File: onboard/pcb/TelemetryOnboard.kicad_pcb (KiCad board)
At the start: 4 copper layers, 100 x 91 mm, 80 parts, among them J1 90 Deg. Socket 02x03 2.54mm, J2 Socket 01x02 2.54mm, J3 CONSMA001-SMD-G-T, J4 Socket 01x04 2.54mm, J5 Socket 01x02 2.54mm, U1 AVR128DB64x-xPT, U2 RC1780HP-RC232

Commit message: first version new schematic
added symbols, footprints, 3dmodels, added new pcb base layout, added first schematic elements
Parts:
- removed C5: 1nF, Capacitor_SMD:C_0805_2012Metric_Pad1.18x1.45mm_HandSolder
- removed D14, D15, D16: LED 0805 red, LED_SMD:LED_0805_2012Metric_Pad1.15x1.40mm_HandSolder
- removed J3: CONSMA001-SMD-G-T, Footprints:SMA Connector CONSMA001-SMD-G-T
- removed J4: Socket 01x04 2.54mm, Connector_PinSocket_2.54mm:PinSocket_1x04_P2.54mm_Vertical
- removed J5: Socket 01x02 2.54mm, Connector_PinSocket_2.54mm:PinSocket_1x02_P2.54mm_Vertical
- removed LS1: CMT-0525-75-SMT-TR, Footprints:Buzzer XDCR_CMT-0525-75-SMT-TR
- removed TP10, TP11, TP12, TP13, TP14, TP15, TP16, TP17, TP4, TP5, TP6, TP7, TP8, TP9: ~, Footprints:Test Point
- removed ZP1, ZS1: ~, Resistor_SMD:R_0805_2012Metric_Pad1.20x1.40mm_HandSolder
- added D3: orange, LED_SMD:LED_0805_2012Metric_Pad1.15x1.40mm_HandSolder, F.Cu at (11.8, 43.0)
- added D4: Cree RGB LED, Footprints:Cree RGB LED, F.Cu at (6.50, 41.0)
- added JP2: SolderJumper_2_Open, Footprints:Solder Jumper, F.Cu at (-20.1, 26.6)
- added R22: 560 Ohm, Resistor_SMD:R_0805_2012Metric, F.Cu at (-35.1, -33.5)
- added REF**: Test Point Hole, Footprints:Test Point Hole, F.Cu at (-24.5, 22.5)
- added REF**: Test Point Hole, Footprints:Test Point Hole, F.Cu at (-10.0, 22.5)
- added REF**: Test Point Hole, Footprints:Test Point Hole, F.Cu at (-13.0, 22.5)
- C1, C3: value 1uF -> 4.7 uF
- C2, C4: value 1uF -> 0.1 uF
- D1, D7: value LED 0805 orange -> orange
- D10: value LED 0805 green -> orange
- D11: value LED 0805 green -> BAT43; footprint LED_SMD:LED_0805_2012Metric_Pad1.15x1.40mm_HandSolder -> Diode_SMD:D_SOD-123
- D12: value LED 0805 green -> green
- D13: value LED 0805 red -> green
- D2: value CLS6B-FKW -> orange; footprint Footprints:RGB LED Cree-PLCC-6_6x5mm_P2.1mm -> LED_SMD:LED_0805_2012Metric_Pad1.15x1.40mm_HandSolder
- D5, D8: value LED 0805 orange -> SP0503BAHT; footprint LED_SMD:LED_0805_2012Metric_Pad1.15x1.40mm_HandSolder -> Package_TO_SOT_SMD:SOT-143
- D6: value LED 0805 orange -> green
- D9: value LED 0805 yellow -> green
- J1: value 90 Deg. Socket 02x03 2.54mm -> USB-C; footprint Connector_PinSocket_2.54mm:PinSocket_2x03_P2.54mm_Horizontal -> Footprints:GCT_USB4215-03-A_REVA
- J2: value Socket 01x02 2.54mm -> USB-C; footprint Connector_PinSocket_2.54mm:PinSocket_1x02_P2.54mm_Vertical -> Footprints:GCT_USB4215-03-A_REVA
- JL1: value Stackable Header 01x08 2.54mm -> Stackable Socket 1x8; footprint Connector_PinSocket_2.54mm:PinSocket_1x08_P2.54mm_Vertical -> Footprints:JL1
- JL2: value Stackable Header 01x06 2.54mm -> Stackable Socket 1x8; footprint Connector_PinSocket_2.54mm:PinSocket_1x06_P2.54mm_Vertical -> Footprints:JL2
- JL3: value ~ -> Stackable Socket 1x8; footprint Connector_PinSocket_2.54mm:PinSocket_1x08_P2.54mm_Vertical -> Footprints:JL3
- JL4: value ~ -> Stackable Socket 1x8; footprint Connector_PinSocket_2.54mm:PinSocket_1x06_P2.54mm_Vertical -> Footprints:JL4
- JP1: value ~ -> SolderJumper_2_Open
- JR1: value Stackable Header 01x08 2.54mm -> Stackable Socket 1x8; footprint Connector_PinSocket_2.54mm:PinSocket_1x08_P2.54mm_Vertical -> Footprints:JR1
- JR2: value Stackable Header 01x06 2.54mm -> Stackable Socket 1x8; footprint Connector_PinSocket_2.54mm:PinSocket_1x06_P2.54mm_Vertical -> Footprints:JR2
- JR3: value ~ -> Stackable Socket 1x8; footprint Connector_PinSocket_2.54mm:PinSocket_1x08_P2.54mm_Vertical -> Footprints:JR3
- JR4: value ~ -> Stackable Socket 1x8; footprint Connector_PinSocket_2.54mm:PinSocket_1x06_P2.54mm_Vertical -> Footprints:JR4
- M1, M2, M3, M4: value ~ -> M4 Mounting Hole
- R1, R11, R12, R2, R3, R4, R5, R6: value 270R -> 560 Ohm; footprint Resistor_SMD:R_0805_2012Metric_Pad1.20x1.40mm_HandSolder -> Resistor_SMD:R_0805_2012Metric
- R10: value 270R -> 22k; footprint Resistor_SMD:R_0805_2012Metric_Pad1.20x1.40mm_HandSolder -> Resistor_SMD:R_0805_2012Metric
- R13, R14: value 1k -> 5k1; footprint Resistor_SMD:R_0805_2012Metric_Pad1.20x1.40mm_HandSolder -> Resistor_SMD:R_0805_2012Metric
- R15: value 1k -> 47k; footprint Resistor_SMD:R_0805_2012Metric_Pad1.20x1.40mm_HandSolder -> Resistor_SMD:R_0805_2012Metric
- R16: value 1k -> 22k; footprint Resistor_SMD:R_0805_2012Metric_Pad1.20x1.40mm_HandSolder -> Resistor_SMD:R_0805_2012Metric
- R17: value 2k7 -> 560 Ohm; footprint Resistor_SMD:R_0805_2012Metric_Pad1.20x1.40mm_HandSolder -> Resistor_SMD:R_0805_2012Metric
- R18, R21: value 5k6 -> 560 Ohm; footprint Resistor_SMD:R_0805_2012Metric_Pad1.20x1.40mm_HandSolder -> Resistor_SMD:R_0805_2012Metric
- R19, R20: value 5k6 -> 470 Ohm; footprint Resistor_SMD:R_0805_2012Metric_Pad1.20x1.40mm_HandSolder -> Resistor_SMD:R_0805_2012Metric
- R7, R8: value 270R -> 5k1; footprint Resistor_SMD:R_0805_2012Metric_Pad1.20x1.40mm_HandSolder -> Resistor_SMD:R_0805_2012Metric
- R9: value 270R -> 47k; footprint Resistor_SMD:R_0805_2012Metric_Pad1.20x1.40mm_HandSolder -> Resistor_SMD:R_0805_2012Metric
- TP1, TP2, TP3: value ~ -> TestPoint
- U1: value AVR128DB64x-xPT -> CP2102N; footprint Package_QFP:TQFP-64_10x10mm_P0.5mm -> Footprints:QFN20_CP2102N_SIL
- U2: value RC1780HP-RC232 -> CP2102N; footprint Footprints:Radiocrafts RC1780HP-RC232 -> Footprints:QFN20_CP2102N_SIL
- moved D9 90.7 mm to (-28.0, 40.1), turned to -90 degrees
- moved D10 88.9 mm to (-31.0, 40.1), turned to -90 degrees
- moved D8 83.5 mm to (-21.5, 35.6), turned to -90 degrees
- moved D7 82.2 mm to (-13.0, 40.1), turned to -90 degrees
- moved D6 81.6 mm to (-10.0, 40.1), turned to -90 degrees
- moved U2 77.1 mm to (-24.5, 31.6), turned to 90 degrees
- moved J2 77.0 mm to (-21.5, 44.8)
- moved D5 75.7 mm to (-3.50, 35.6), turned to -90 degrees
- moved R7 73.3 mm to (-7.00, 38.1)
- moved R14 70.2 mm to (-18.0, 38.1), turned to 0 degrees
- moved R10 68.8 mm to (0.91, 33.6), turned to 90 degrees
- moved R8 68.5 mm to (0.00, 38.1), turned to 0 degrees
- moved R9 67.8 mm to (0.91, 28.6), turned to 90 degrees
- moved R21 67.5 mm to (-35.0, -37.0), turned to 180 degrees
- moved R5 66.6 mm to (6.50, 33.0), turned to -90 degrees
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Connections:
- net SCL2 renamed D5
- net SDA2 renamed D4
- C2 pad 1: GND -> +3V3
- C2 pad 2: +3V3 -> GND
- C4 pad 1: GND -> +3V3
- C4 pad 2: +3V3 -> GND
- D10 pad 1: GND -> Net-(D10-K)
- D10 pad 2: Net-(D10-A) -> +3V3
- D11 pad 1: GND -> Net-(D11-K)
- D13 pad 1: Net-(D13-K) -> GND
- D13 pad 2: +3V3 -> Net-(D13-A)
- D2 pad 1: Net-(D2-AR) -> GND
- D2 pad 2: Net-(D2-AG) -> Net-(D2-A)
- D5 pad 2: Net-(D5-A) -> VBUS1
- D6 pad 1: GND -> Net-(D6-K)
- D6 pad 2: Net-(D6-A) -> +3V3
- D7 pad 1: GND -> Net-(D7-K)
- D7 pad 2: Net-(D7-A) -> +3V3
- D8 pad 2: Net-(D8-A) -> VBUS2
- D9 pad 1: GND -> Net-(D9-K)
- D9 pad 2: Net-(D9-A) -> +3V3
- JL1 pad 1: SDA0 -> SDA
- JL1 pad 2: SCL0 -> SCL
- JL1 pad 7: D1 -> RX_BUS
- JL1 pad 8: D2 -> TX_BUS
- JL3 pad 1: SDA0 -> SDA
- JL3 pad 2: SCL0 -> SCL
- JL3 pad 7: D1 -> RX_BUS
- JL3 pad 8: D2 -> TX_BUS
- JP1 pad 2: +5V -> GND
- JR1 pad 25: VCC_B -> GND
- JR1 pad 26: GND -> D26
- JR1 pad 27: SLP -> D27
- JR1 pad 28: ARM -> D28
- JR2 pad 17: +5V -> +3V_LP
- JR2 pad 18: +3V3 -> +V_BATT
- JR2 pad 19: +3V3 -> +5V
- JR2 pad 20: +3V3 -> +5V
- JR3 pad 25: VCC_B -> GND
- JR3 pad 26: GND -> D26
- JR3 pad 27: SLP -> D27
- JR3 pad 28: ARM -> D28
- JR4 pad 17: +5V -> +3V_LP
- JR4 pad 18: +3V3 -> +V_BATT
- JR4 pad 19: +3V3 -> +5V
- JR4 pad 20: +3V3 -> +5V
- R1 pad 1: LED EV -> LED 1
- R10 pad 1: Net-(D10-A) -> VBUS1
- R10 pad 2: Net-(U2-D1) -> Net-(U1-VBUS)
- R11 pad 1: +3V3 -> Net-(D6-K)
- R11 pad 2: Net-(D11-A) -> Net-(U1-~{TXT}/GPIO.2)
- R12 pad 1: +5V -> Net-(D7-K)
- R12 pad 2: Net-(D12-A) -> Net-(U1-~{RXT}/GPIO.3)
- R13 pad 1: Net-(D13-K) -> Net-(J2-CC1)
- R13 pad 2: TX0 -> GND
- R14 pad 1: RX0 -> Net-(J2-CC2)
- R14 pad 2: Net-(D14-K) -> GND
- R15 pad 1: Net-(D15-K) -> Net-(U2-VBUS)
- R15 pad 2: TX4 -> GND
- R16 pad 1: RX4 -> VBUS2
- R16 pad 2: Net-(D16-K) -> Net-(U2-VBUS)
- R17 pad 1: Net-(U2-RESET) -> Net-(D9-K)
- R17 pad 2: RST -> Net-(U2-~{TXT}/GPIO.2)
- R18 pad 1: +3V3 -> Net-(D10-K)
- R18 pad 2: RST -> Net-(U2-~{RXT}/GPIO.3)
- R19 pad 1: +3V3 -> Net-(D11-K)
- R19 pad 2: TX0 -> Net-(U2-TXD)
- R2 pad 1: LED R -> LED 2
- R2 pad 2: Net-(D2-AR) -> Net-(D2-A)
- R20 pad 1: +3V3 -> UPDI
- R20 pad 2: CFG -> Net-(D11-A)
- R21 pad 1: ARM -> +3V3
- R21 pad 2: GND -> Net-(D12-A)
- R3 pad 1: LED G -> LED 3
- R3 pad 2: Net-(D2-AG) -> Net-(D3-A)
- R4 pad 1: LED B -> LED R
- R4 pad 2: Net-(D2-AB) -> Net-(D4-AR)
- R5 pad 1: Net-(D5-A) -> LED G
- R5 pad 2: Net-(U1-PF2) -> Net-(D4-AG)
- R6 pad 1: Net-(D6-A) -> LED B
- R6 pad 2: Net-(U1-PE7) -> Net-(D4-AB)
- R7 pad 1: Net-(D7-A) -> Net-(J1-CC1)
- R7 pad 2: Net-(U1-PE5) -> GND
- R8 pad 1: Net-(D8-A) -> Net-(J1-CC2)
- R8 pad 2: Net-(U1-PE3) -> GND
- R9 pad 1: Net-(D9-A) -> Net-(U1-VBUS)
- R9 pad 2: Net-(U2-D2) -> GND
- TP1 pad 1: RST -> RX
- TP2 pad 1: CFG -> TX
- TP3 pad 1: TX0 -> UPDI
- U1 pad 12: Net-(U1-PB4) -> GND
- U1 pad 13: CTS -> unconnected-(U1-~{WAKEUP}-Pad13)
- U1 pad 14: CFG -> unconnected-(U1-SUSPEND-Pad14)
- U1 pad 15: RTS -> Net-(JP1-A)
- U1 pad 16: TX1 -> unconnected-(U1-~{RTS}-Pad16)
- U1 pad 17: RX1 -> TX
- U1 pad 18: SDA0 -> RX
- U1 pad 19: SCL0 -> Net-(U1-~{RXT}/GPIO.3)
- U1 pad 2: TX0 -> unconnected-(U1-CLK/GPIO.0-Pad2)
- U1 pad 20: +3V3 -> Net-(U1-~{TXT}/GPIO.2)
- U1 pad 3: RX0 -> GND
- U1 pad 4: unconnected-(U1-PA6-Pad4) -> D+1
- U1 pad 5: unconnected-(U1-PA7-Pad5) -> D-1
- U1 pad 7: GND -> +3V3
- U1 pad 8: unconnected-(U1-PB0-Pad8) -> Net-(U1-VBUS)
- U2 pad 1: GND -> unconnected-(U2-RS485/GPIO.1-Pad1)
- U2 pad 10: GND -> unconnected-(U2-NC-Pad10)
- U2 pad 12: Net-(U2-RESET) -> GND
- U2 pad 13: +3V3 -> unconnected-(U2-~{WAKEUP}-Pad13)
- U2 pad 14: GND -> unconnected-(U2-SUSPEND-Pad14)
- U2 pad 15: unconnected-(U2-Pad15) -> Net-(JP2-A)
- U2 pad 17: unconnected-(U2-Pad17) -> Net-(D11-A)
- U2 pad 18: unconnected-(U2-Pad18) -> Net-(U2-TXD)
- U2 pad 19: Net-(J2-Pin_1) -> Net-(U2-~{RXT}/GPIO.3)
- U2 pad 2: CTS -> unconnected-(U2-CLK/GPIO.0-Pad2)
- U2 pad 20: Net-(J2-Pin_2) -> Net-(U2-~{TXT}/GPIO.2)
- U2 pad 21: unconnected-(U2-Pad21) -> GND
- U2 pad 3: RTS -> GND
- U2 pad 4: CFG -> D+2
- U2 pad 5: RX0 -> D-2
- U2 pad 6: TX0 -> +3V3
- U2 pad 7: GND -> +3V3
- U2 pad 8: GND -> Net-(U2-VBUS)
- U2 pad 9: Net-(U2-RF) -> unconnected-(U2-~{RST}-Pad9)
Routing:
- net ARM: track 116.1 -> 0.00 mm, vias 2 -> 0
- net D3: track 111.1 -> 0.00 mm, vias 1 -> 0
- net SLP: track 114.9 -> 4.87 mm, vias 1 -> 0
- net Net-(U1-PE3): track 102.4 -> 0.00 mm, vias 2 -> 0
- net Net-(U1-PE5): track 101.9 -> 0.00 mm, vias 2 -> 0
- net Net-(U1-PE7): track 101.3 -> 0.00 mm, vias 2 -> 0
- net Net-(U1-PF2): track 100.6 -> 0.00 mm, vias 2 -> 0
- net +5V: track 110.6 -> 38.1 mm, vias 3 -> 0
- net RST: track 66.6 -> 0.00 mm, vias 2 -> 0
- net GND: track 65.9 -> 6.25 mm, vias 296 -> 136
- net RTS: track 49.5 -> 0.00 mm, vias 2 -> 0
- net CFG: track 48.4 -> 0.00 mm, vias 2 -> 0
- net CTS: track 47.3 -> 0.00 mm, vias 2 -> 0
- net RX0: track 43.0 -> 0.00 mm
- net LED EV: track 40.9 -> 0.00 mm
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- removed copper zone on In2.Cu, net +3V3
- removed copper zone on In2.Cu, net +5V
- removed copper zone on In1.Cu, net GND
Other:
- board size 100 x 91 mm -> 95 x 95 mm
- copper layers 4 -> 2
- board text added: "0x??"
- board text added: "29"
- board text added: "30"
- board text added: "31"
- board text added: "32"
- board text added: "ARM1"
- board text added: "ARM2"
- board text added: "BAT"
- board text added: "D26"
- board text added: "D27"
- board text added: "D28"
- board text added: "D5"
- board text added: "LP"
- board text added: "PWR"
- board text added: "RX"
- board text added: "SPROG ASCENT III MODUL vx.y.z"
- board text added: "Serial Number:"
- board text added: "TX"
- board text added: "UART"
- board text added: "UPDI"
- board text removed: "0x10"
- board text removed: "ARM"
- board text removed: "Bridge the 5V jumper only for RC1780HP"
- board text removed: "C"
- board text removed: "D1"
- board text removed: "D2"
- board text removed: "D3"
- board text removed: "DC"
- board text removed: "DD"
- board text removed: "Giessen, 2025/09/01"
- board text removed: "I"
- board text removed: "JLCJLCJLCJLC"
- board text removed: "L"
- board text removed: "Licensed under CERN-OHL-S v2 or any later version: ohwr.org/cern_ohl_s_v2.txt The source files can be found at: github.com/Spaceflight-Rocketry-Giessen-e-V/Telemetry"
- board text removed: "O"
- board text removed: "R"
- board text removed: "RX_L"
- board text removed: "S"
- board text removed: "SCL2"
- board text removed: "SDA2"
- board text removed: "SPROG ASCENT II TELEMETRY v0.0.1"
- board text removed: "TX RX UPDI 3V3 GND GND"
- board text removed: "TX_L"
- board text removed: "UPDI RX TX GND GND 3V3"
- board text removed: "VCC_B"

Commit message: update platine
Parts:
- added C10: 0805 1uF, Capacitor_SMD:C_0805_2012Metric_Pad1.18x1.45mm_HandSolder, F.Cu at (34.8, -155.8)
- added C11: 0805 1uF, Capacitor_SMD:C_0805_2012Metric_Pad1.18x1.45mm_HandSolder, F.Cu at (34.8, -152.8)
- added C12: 0805 1uF, Capacitor_SMD:C_0805_2012Metric_Pad1.18x1.45mm_HandSolder, F.Cu at (34.8, -149.8)
- added C15: 1 uf, Capacitor_SMD:C_0805_2012Metric_Pad1.18x1.45mm_HandSolder, F.Cu at (34.8, -146.8)
- added C5: 0805 1nF, Capacitor_SMD:C_0805_2012Metric_Pad1.18x1.45mm_HandSolder, F.Cu at (-12.0, -18.0)
- added C6: 1 uf, Capacitor_SMD:C_0805_2012Metric_Pad1.18x1.45mm_HandSolder, F.Cu at (-12.0, -15.0)
- added C7: 0805 1nF, Capacitor_SMD:C_0805_2012Metric_Pad1.18x1.45mm_HandSolder, F.Cu at (-12.0, -12.0)
- added C8: 1 uf, Capacitor_SMD:C_0805_2012Metric_Pad1.18x1.45mm_HandSolder, F.Cu at (-12.0, -8.98)
- added C9: 0805 1uF, Capacitor_SMD:C_0805_2012Metric_Pad1.18x1.45mm_HandSolder, F.Cu at (34.8, -158.8)
- added D14: LED 0805 green, LED_SMD:LED_0805_2012Metric_Pad1.15x1.40mm_HandSolder, F.Cu at (5.84, -138.3)
- added D15: LED 0805 yellow, LED_SMD:LED_0805_2012Metric_Pad1.15x1.40mm_HandSolder, F.Cu at (5.84, -135.2)
- added D16: LED 0805 green, LED_SMD:LED_0805_2012Metric_Pad1.15x1.40mm_HandSolder, F.Cu at (5.84, -132.2)
- added D17: LED 0805 yellow, LED_SMD:LED_0805_2012Metric_Pad1.15x1.40mm_HandSolder, F.Cu at (5.84, -129.1)
- added D18: D, Diode_SMD:D_SOD-123, F.Cu at (57.1, -153.0)
- added D19: LED 0805 red, LED_SMD:LED_0805_2012Metric_Pad1.15x1.40mm_HandSolder, F.Cu at (5.84, -126.1)
- added D20: LED 0805 red, LED_SMD:LED_0805_2012Metric_Pad1.15x1.40mm_HandSolder, F.Cu at (10.6, -138.3)
- added D21: LED 0805 red, LED_SMD:LED_0805_2012Metric_Pad1.15x1.40mm_HandSolder, F.Cu at (10.6, -135.2)
- added D22: LED 0805 red, LED_SMD:LED_0805_2012Metric_Pad1.15x1.40mm_HandSolder, F.Cu at (10.6, -132.2)
- added D23: LED 0805 red, LED_SMD:LED_0805_2012Metric_Pad1.15x1.40mm_HandSolder, F.Cu at (10.6, -129.1)
- added D24: LED 0805 red, LED_SMD:LED_0805_2012Metric_Pad1.15x1.40mm_HandSolder, F.Cu at (10.6, -126.1)
- added D25: LED 0805 orange, LED_SMD:LED_0805_2012Metric_Pad1.15x1.40mm_HandSolder, F.Cu at (15.4, -138.3)
- added D26: LED 0805 orange, LED_SMD:LED_0805_2012Metric_Pad1.15x1.40mm_HandSolder, F.Cu at (15.4, -135.2)
- added D27: LED 0805 orange, LED_SMD:LED_0805_2012Metric_Pad1.15x1.40mm_HandSolder, F.Cu at (-20.5, 8.00)
- added D28: LED 0805 orange, LED_SMD:LED_0805_2012Metric_Pad1.15x1.40mm_HandSolder, F.Cu at (15.4, -129.1)
- added J3: CONSMA001-SMD-G-T, Footprints:SMA Connector CONSMA001-SMD-G-T, F.Cu at (0.00, 0.00)
- added J4: CONSMA001-SMD-G-T, Footprints:SMA Connector CONSMA001-SMD-G-T, F.Cu at (20.0, 0.00)
- added LS1: Buzzer CMT-0525-75-SMT-TR, Footprints:Buzzer XDCR_CMT-0525-75-SMT-TR, F.Cu at (-23.8, 15.6)
- added Q1: NPN, Package_TO_SOT_SMD:SOT-23, F.Cu at (56.6, -148.9)
- added R23: 0805 2k7, Resistor_SMD:R_0805_2012Metric_Pad1.20x1.40mm_HandSolder, F.Cu at (-25.5, -37.0)
- added R24: 0805 270R, Resistor_SMD:R_0805_2012Metric_Pad1.20x1.40mm_HandSolder, F.Cu at (39.6, -167.9)
- added R25: 0805 270R, Resistor_SMD:R_0805_2012Metric_Pad1.20x1.40mm_HandSolder, F.Cu at (39.6, -165.0)
- added R26: 0805 2k7, Resistor_SMD:R_0805_2012Metric_Pad1.20x1.40mm_HandSolder, F.Cu at (-25.5, -43.0)
- added R27: 0805 270R, Resistor_SMD:R_0805_2012Metric_Pad1.20x1.40mm_HandSolder, F.Cu at (39.6, -159.1)
- added R28: 0805 270R, Resistor_SMD:R_0805_2012Metric_Pad1.20x1.40mm_HandSolder, F.Cu at (39.6, -156.1)
- added R29: 180 R, Resistor_SMD:R_0805_2012Metric_Pad1.20x1.40mm_HandSolder, F.Cu at (44.3, -170.9)
- added R30: 10kR, Resistor_SMD:R_0805_2012Metric_Pad1.20x1.40mm_HandSolder, F.Cu at (44.3, -167.9)
- added R31: 10kR, Resistor_SMD:R_0805_2012Metric_Pad1.20x1.40mm_HandSolder, F.Cu at (44.3, -165.0)
- added R32: 0805 1k, Resistor_SMD:R_0805_2012Metric_Pad1.20x1.40mm_HandSolder, F.Cu at (-16.5, -31.5)
- added R33: 0805 1k, Resistor_SMD:R_0805_2012Metric_Pad1.20x1.40mm_HandSolder, F.Cu at (-11.5, -29.5)
- added R34: 0805 5k6, Resistor_SMD:R_0805_2012Metric_Pad1.20x1.40mm_HandSolder, F.Cu at (-11.5, -24.5)
- added R35: 0805 1k, Resistor_SMD:R_0805_2012Metric_Pad1.20x1.40mm_HandSolder, F.Cu at (-11.8, -40.4)
- added R36: 0805 1k, Resistor_SMD:R_0805_2012Metric_Pad1.20x1.40mm_HandSolder, F.Cu at (-11.8, -37.4)
- added R37: 0805 5k6, Resistor_SMD:R_0805_2012Metric_Pad1.20x1.40mm_HandSolder, F.Cu at (-11.8, -34.5)
- added R38: 0805 5k6, Resistor_SMD:R_0805_2012Metric_Pad1.20x1.40mm_HandSolder, F.Cu at (-16.0, -43.0)
- added R39: 0805 5k6, Resistor_SMD:R_0805_2012Metric_Pad1.20x1.40mm_HandSolder, F.Cu at (-16.0, -40.0)
- added R40: 0805 5k6, Resistor_SMD:R_0805_2012Metric_Pad1.20x1.40mm_HandSolder, F.Cu at (-16.0, -37.1)
- added R41: 0805 5k6, Resistor_SMD:R_0805_2012Metric_Pad1.20x1.40mm_HandSolder, F.Cu at (-23.5, -33.0)
- added R42: 5.6kR, Resistor_SMD:R_0805_2012Metric_Pad1.20x1.40mm_HandSolder, F.Cu at (53.8, -167.9)
- added R43: 0805 1k, Resistor_SMD:R_0805_2012Metric_Pad1.20x1.40mm_HandSolder, F.Cu at (53.8, -165.0)
- added R44: 0805 1k, Resistor_SMD:R_0805_2012Metric_Pad1.20x1.40mm_HandSolder, F.Cu at (53.8, -162.0)
- added R45: 0805 270R, Resistor_SMD:R_0805_2012Metric_Pad1.20x1.40mm_HandSolder, F.Cu at (53.8, -159.1)
- added R46: 0805 270R, Resistor_SMD:R_0805_2012Metric_Pad1.20x1.40mm_HandSolder, F.Cu at (53.8, -156.1)
- added R47: 0805 270R, Resistor_SMD:R_0805_2012Metric_Pad1.20x1.40mm_HandSolder, F.Cu at (-21.5, 2.00)
- added R48: 0805 270R, Resistor_SMD:R_0805_2012Metric_Pad1.20x1.40mm_HandSolder, F.Cu at (58.6, -167.9)
- added TP12: TestPoint, Footprints:Test Point, F.Cu at (34.4, -127.0)
- added TP13: TestPoint, Footprints:Test Point, F.Cu at (38.5, -143.2)
- added TP14: TestPoint, Footprints:Test Point, F.Cu at (38.5, -139.2)
- added TP15: TestPoint, Footprints:Test Point, F.Cu at (38.5, -135.1)
- added TP16: ~, Footprints:Test Point, F.Cu at (-13.5, -0.55)
- added TP17: ~, Footprints:Test Point, F.Cu at (-13.5, 3.50)
- added TP18: TestPoint, Footprints:Test Point, F.Cu at (42.5, -143.2)
- added TP19: TestPoint, Footprints:Test Point, F.Cu at (42.5, -139.2)
- added TP36: TestPoint, Footprints:Test Point, F.Cu at (42.5, -135.1)
- added TP37: TestPoint, Footprints:Test Point, F.Cu at (42.5, -131.1)
- added TP38: TestPoint, Footprints:Test Point, F.Cu at (42.5, -127.0)
- added TP39: TestPoint, Footprints:Test Point, F.Cu at (46.6, -143.2)
- added TP4: TestPoint, Footprints:Test Point, F.Cu at (34.4, -143.2)
- added TP40: ~, Footprints:Test Point, F.Cu at (46.6, -139.2)
- added TP41: TestPoint, Footprints:Test Point, F.Cu at (46.6, -135.1)
- added TP42: ~, Footprints:Test Point, F.Cu at (46.6, -131.1)
- added TP5: TestPoint, Footprints:Test Point, F.Cu at (34.4, -139.2)
- added TP8: TestPoint, Footprints:Test Point, F.Cu at (34.4, -135.1)
- added TP9: TestPoint, Footprints:Test Point, F.Cu at (34.4, -131.1)
- added U3: RC1780HP-RC232, Footprints:Radiocrafts RC1780HP-RC232, F.Cu at (8.89, -37.4)
- added U4: RC1701HP-RC232, Footprints:Radiocrafts RC1780HP-RC232, F.Cu at (28.9, -37.4)
- added U5: AVR128DB64x-xPT, Package_QFP:TQFP-64_10x10mm_P0.5mm, F.Cu at (-22.8, -17.2)
- added U6: W25Q80DVSSIG, Package_SO:SOIC-8_5.3x5.3mm_P1.27mm, F.Cu at (14.0, 15.2)
- added ZP1: ~, Resistor_SMD:R_0805_2012Metric_Pad1.20x1.40mm_HandSolder, F.Cu at (-1.00, -5.50)
- added ZP2: ~, Resistor_SMD:R_0805_2012Metric_Pad1.20x1.40mm_HandSolder, F.Cu at (19.0, -5.50)
- added ZS1: ~, Resistor_SMD:R_0805_2012Metric_Pad1.20x1.40mm_HandSolder, F.Cu at (0.00, -8.50)
- added ZS2: ~, Resistor_SMD:R_0805_2012Metric_Pad1.20x1.40mm_HandSolder, F.Cu at (20.0, -8.50)
- R1, R10, R11, R12, R13, R14, R15, R16, R17, R18, R19, R2, R20, R21, R22, R3, R4, R5, R6, R7, R8, R9: footprint Resistor_SMD:R_0805_2012Metric -> Resistor_SMD:R_0805_2012Metric_Pad1.20x1.40mm_HandSolder
- TP2, TP3: value TestPoint -> ~
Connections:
- net SCL renamed SCL1
- net SDA renamed SDA1
- TP1 pad 1: RX -> RST1
- TP2 pad 1: TX -> TX0
- TP3 pad 1: UPDI -> RX0
- U1 pad 17: TX -> TX4
- U1 pad 18: RX -> RX4
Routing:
- net +5V: track 38.1 -> 39.7 mm, vias 0 -> 1
- net +3V3: track 57.9 -> 59.4 mm, vias 4 -> 5
- added copper zone on In2.Cu, net +3V3
- added copper zone on In1.Cu, net GND
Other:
- copper layers 2 -> 4

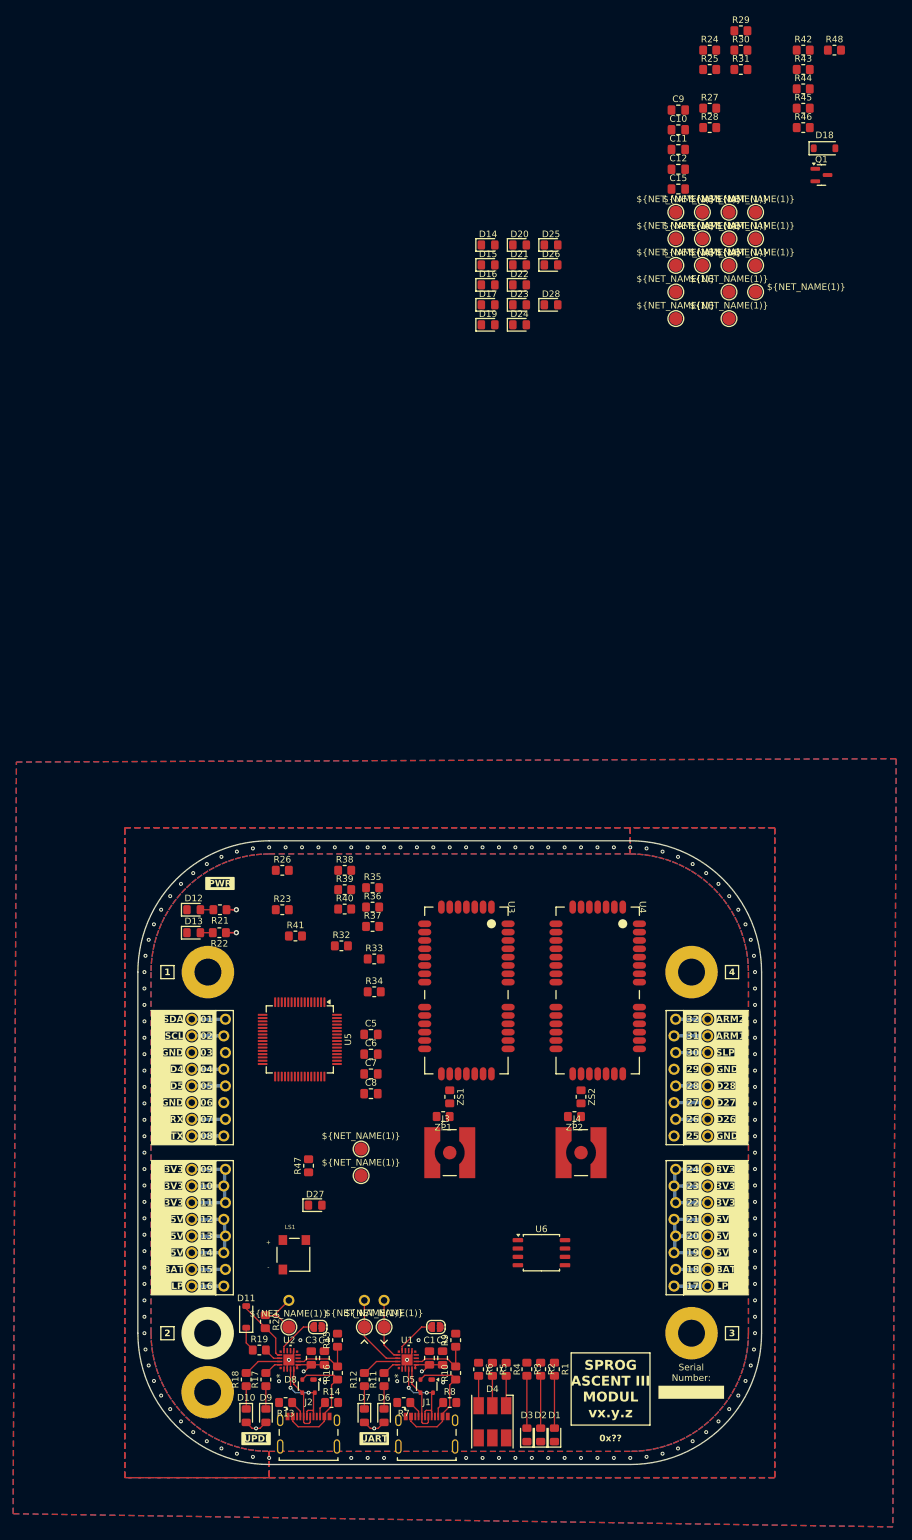
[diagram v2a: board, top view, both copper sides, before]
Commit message: update platine radio module led
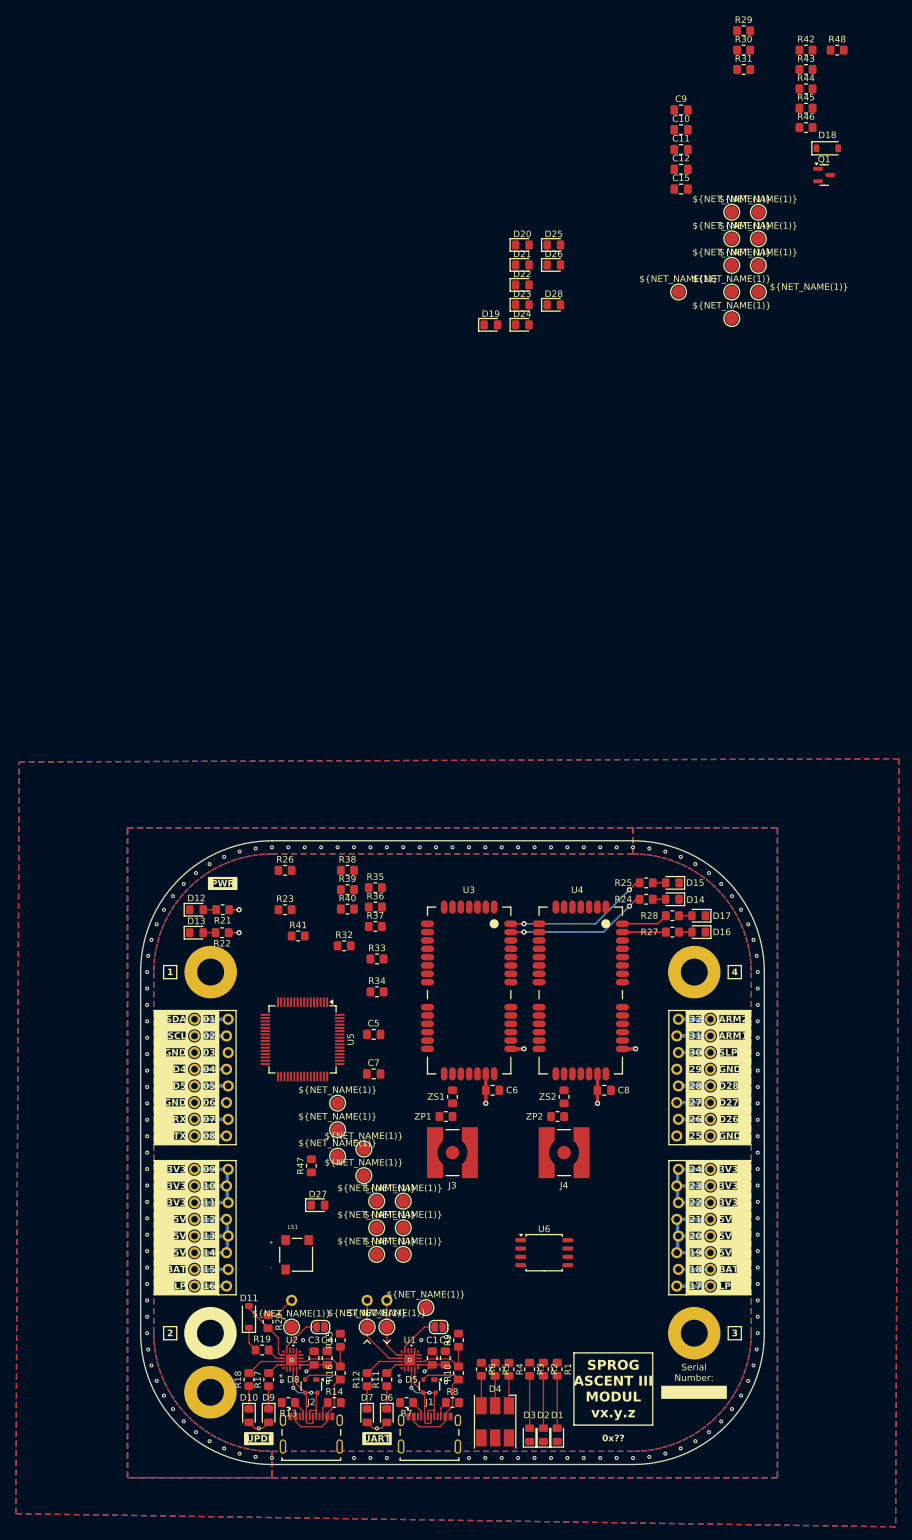
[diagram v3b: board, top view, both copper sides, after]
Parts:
- added TP60: TestPoint, Footprints:Test Point, F.Cu at (-17.1, -7.55)
- added TP70: ~, Footprints:Test Point, F.Cu at (-17.1, -3.50)
- added TP80: ~, Footprints:Test Point, F.Cu at (-17.1, 0.55)
- TP2, TP3: value ~ -> TestPoint
- moved TP13 157.4 mm to (-7.08, 7.40)
- moved TP4 157.4 mm to (-11.1, 7.40)
- moved TP14 157.4 mm to (-7.08, 11.4)
- moved TP15 157.4 mm to (-7.08, 15.5)
- moved TP5 157.4 mm to (-11.1, 11.4)
- moved TP8 157.4 mm to (-11.1, 15.5)
- moved TP12 155.4 mm to (-3.63, 23.6)
- moved R27 134.5 mm to (33.9, -33.6), turned to 180 degrees
- moved R28 129.0 mm to (33.9, -36.1), turned to 180 degrees
- moved R24 120.9 mm to (29.9, -38.6), turned to 180 degrees
- moved R25 115.4 mm to (29.9, -41.1), turned to 180 degrees
- moved D16 109.5 mm to (37.9, -33.6), turned to 180 degrees
- moved D17 104.2 mm to (37.9, -36.1), turned to 180 degrees
- moved D14 97.7 mm to (33.9, -38.6), turned to 180 degrees
- moved D15 92.4 mm to (33.9, -41.1), turned to 180 degrees
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- renumbered D16 to D14, D17 to D15, D14 to D16, D15 to D17, R27 to R24, R28 to R25, R24 to R27, R25 to R28
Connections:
- R24 pad 2: Net-(U4-D1) -> Net-(U3-D1)
- R25 pad 2: Net-(U4-D2) -> Net-(U3-D2)
- R27 pad 2: Net-(U3-D1) -> Net-(U4-D1)
- R28 pad 2: Net-(U3-D2) -> Net-(U4-D2)
- TP1 pad 1: RST1 -> RX4
- TP2 pad 1: TX0 -> TX4
- TP3 pad 1: RX0 -> UPDI
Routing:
- net Net-(U3-D2): track 0.00 -> 22.2 mm, vias 0 -> 2
- net Net-(U3-D1): track 0.00 -> 21.7 mm, vias 0 -> 2
- net +3V3: track 59.4 -> 70.4 mm, vias 5 -> 8
- net Net-(U4-D2): track 0.00 -> 7.12 mm
- net Net-(U4-D1): track 0.00 -> 6.61 mm
- net +5V: track 39.7 -> 41.7 mm, vias 1 -> 2
- net Net-(D17-A): track 0.00 -> 1.98 mm
- net Net-(D16-A): track 0.00 -> 1.98 mm
- net Net-(D15-A): track 0.00 -> 1.98 mm
- net Net-(D14-A): track 0.00 -> 1.98 mm
